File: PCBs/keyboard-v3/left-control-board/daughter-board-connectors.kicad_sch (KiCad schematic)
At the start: 2 parts, among them J601 F31Z1A7H111008, J602 F31Z1A7H111008

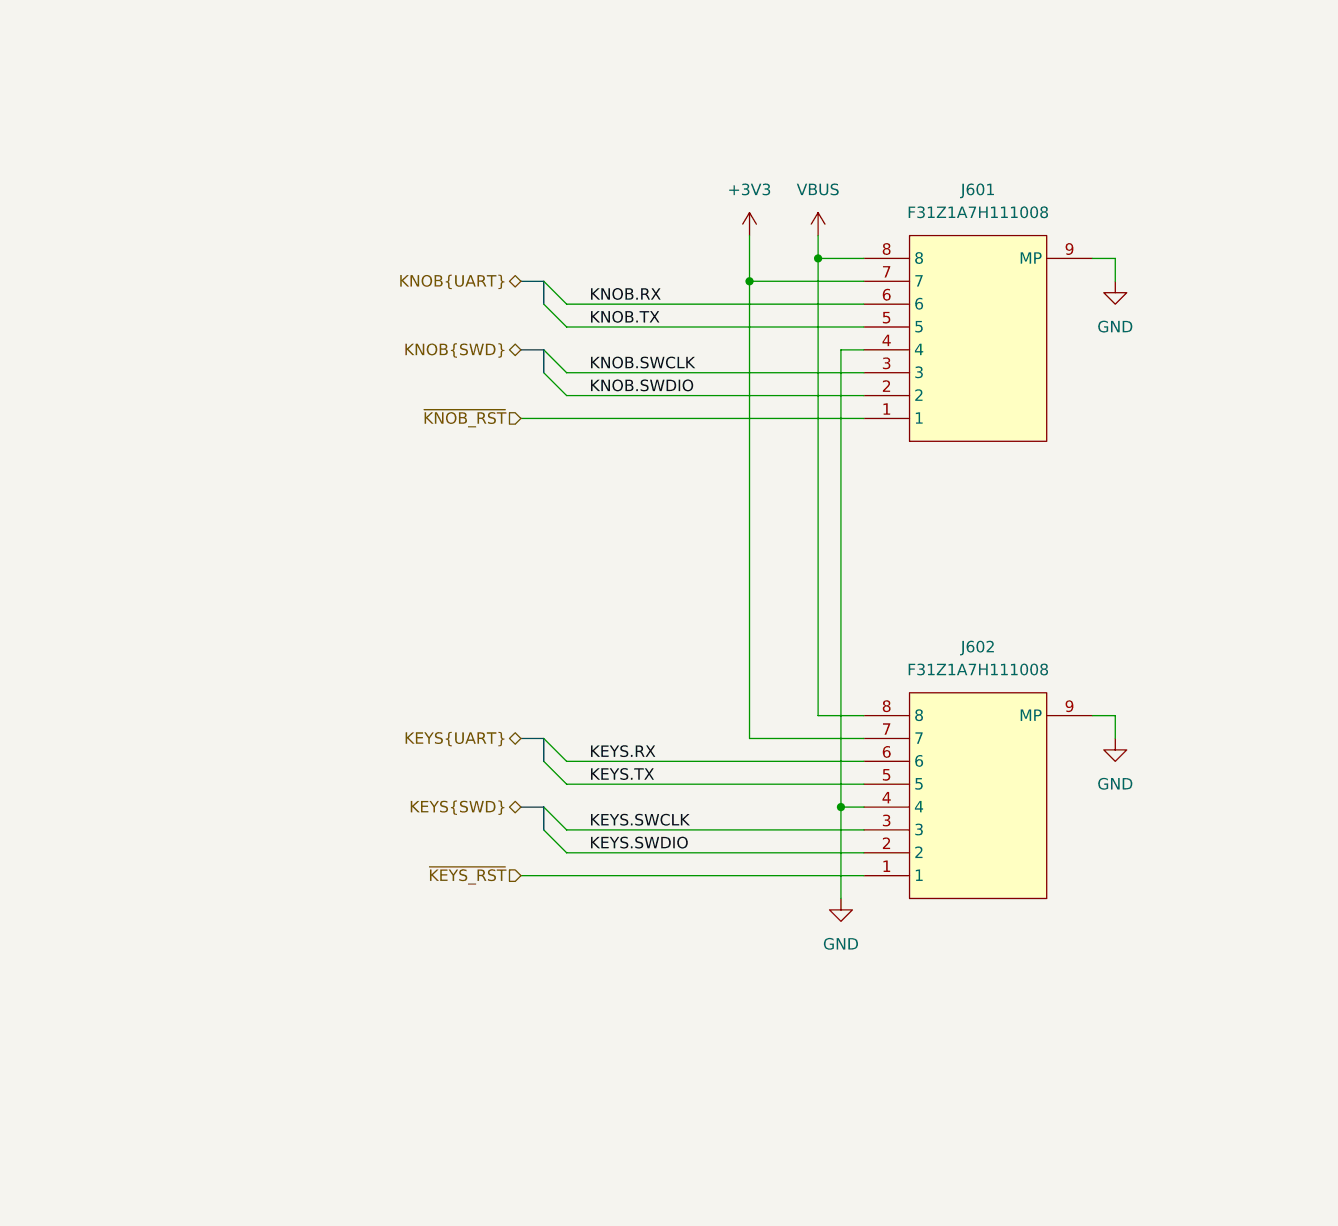
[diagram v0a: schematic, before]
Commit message: Left knob board done
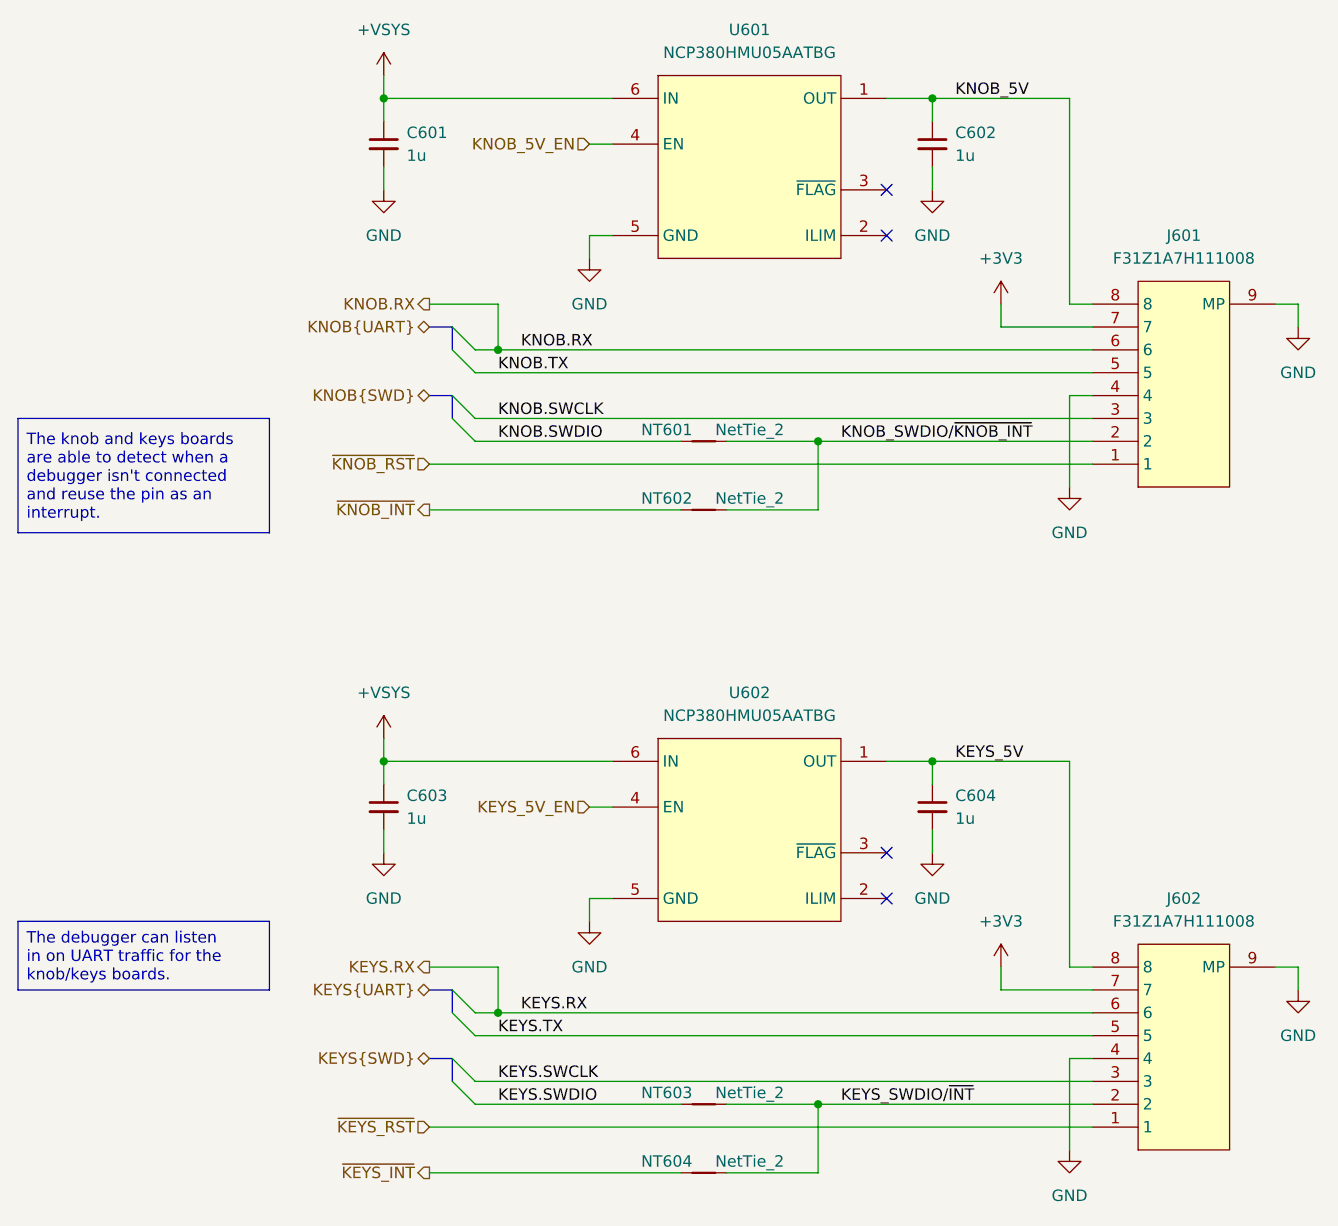
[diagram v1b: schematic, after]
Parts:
- added C601, C602, C603, C604: 1u, project_footprints:C_0402, symbol DEV:C_SMALL
- added NT601, NT602, NT603, NT604: NetTie_2, project_footprints:NetTie-2_SMD_Pad0.15mm, symbol Device:NetTie_2
- added U601, U602: NCP380HMU05AATBG, project_footprints:SON65P200X200X55-7N, symbol PWR-SWCH:NCP380HMU05AATBG
- J601, J602: symbol CONN-FPC:F31Z1A7H111008 -> CONN-FPC:F31Z-1A7H1-11008
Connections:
- net GND: now also C601.2, C602.2, C603.2, C604.2, U601.5 (GND), U601.7 (GND), U602.5 (GND), U602.7 (GND)
- net KEYS.SWDIO: now also NT603.1; no longer J602.2
- net KNOB.SWDIO: now also NT601.1; no longer J601.2
- net VBUS renamed KEYS_5V
- net KEYS_5V: now also C604.1, U602.1 (OUT); no longer J601.8
- new net +VSYS: C601.1, C603.1, U601.6 (IN), U602.6 (IN)
- new net KEYS_5V_EN: U602.4 (EN)
- new net KEYS_SWDIO/~{INT}: J602.2, NT603.2, NT604.2
- new net KNOB_5V: C602.1, J601.8, U601.1 (OUT)
- new net KNOB_5V_EN: U601.4 (EN)
- new net KNOB_SWDIO/~{KNOB_INT}: J601.2, NT601.2, NT602.2
- new net ~{KEYS_INT}: NT604.1
- new net ~{KNOB_INT}: NT602.1
- no-connect marks 0 -> 4
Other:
- moved on the sheet: J601, J602
